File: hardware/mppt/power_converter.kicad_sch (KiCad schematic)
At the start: 25 parts, among them J301 Conn_01x01, J302 Conn_01x01, J303 CT3151, J304 CT3151, J305 CT3151, J306 CT3151, J307 Conn_01x01, J308 Conn_01x01

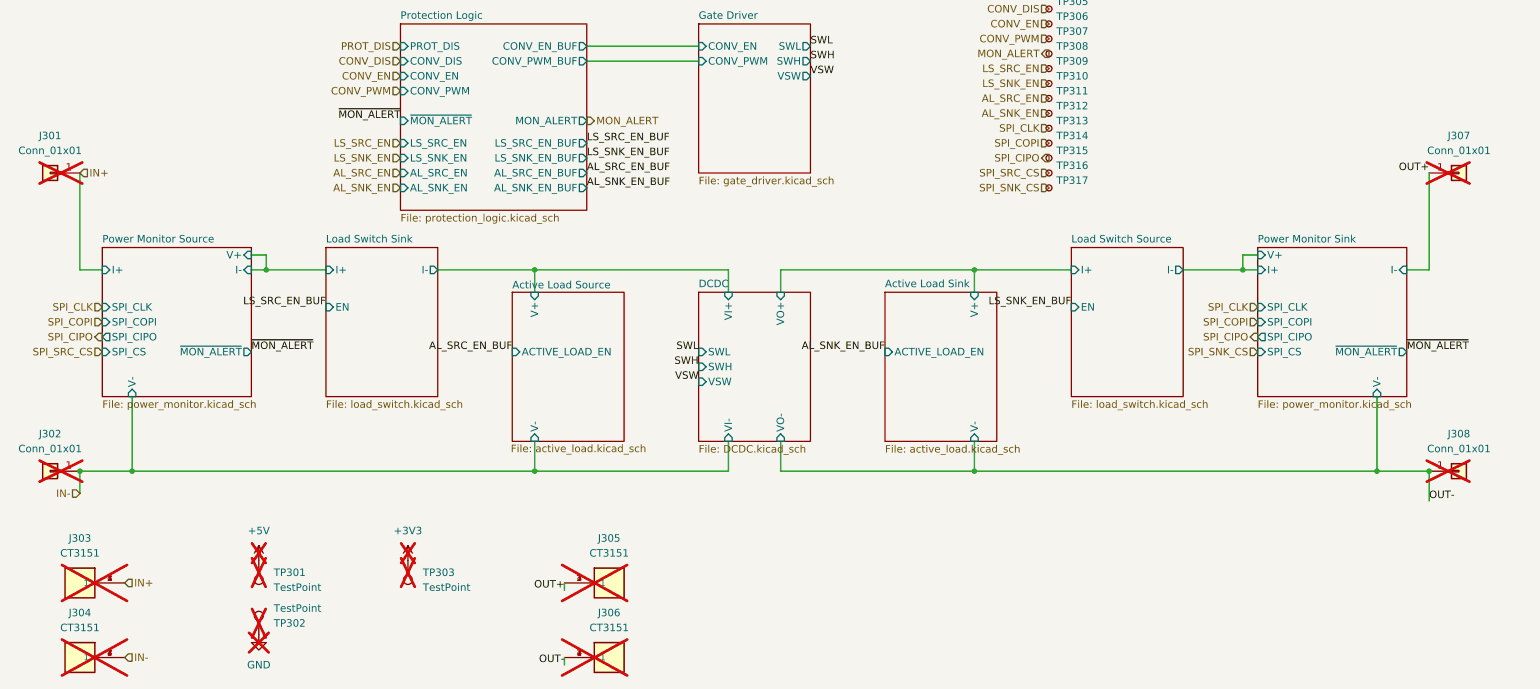
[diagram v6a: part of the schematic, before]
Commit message: converter schematic and layout.
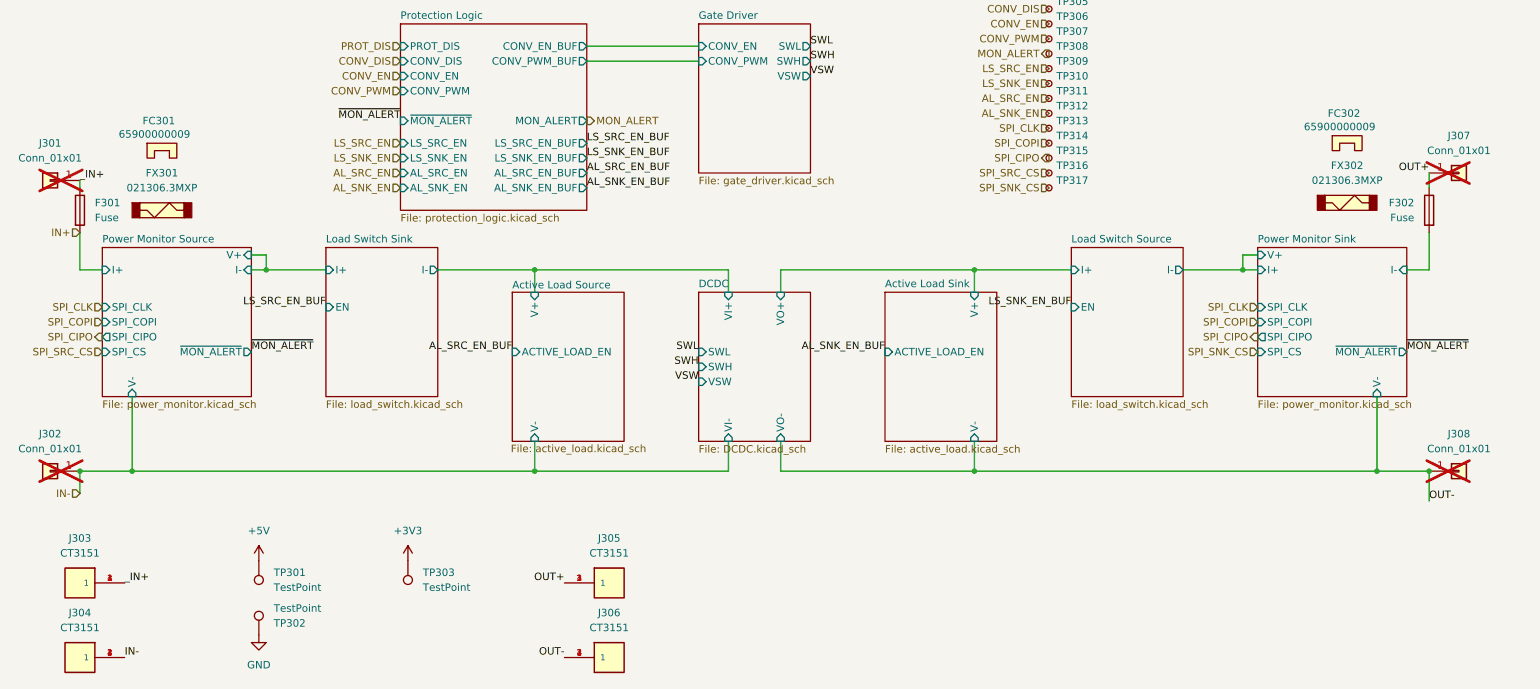
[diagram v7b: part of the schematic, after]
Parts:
- added F301, F302: Fuse, footprints:littelfuse_65600001009, symbol Device:Fuse
- added FC301, FC302: 65900000009, symbol littelfuse_021306_3MXP:65900000009
- added FX301, FX302: 021306.3MXP, symbol littelfuse_021306_3MXP:021306_3MXP
- J303, J304, J305, J306, TP301, TP302, TP303: now fitted; now in the parts list
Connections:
- net IN+: now also F301.2; no longer J301.1 (Pin_1), J303.1, J303.2 (1), J303.3 (1), J303.4 (1)
- net OUT+: now also F302.1
- new net Power Monitor Sink/I-: F302.2
- new net _IN+: F301.1, J301.1 (Pin_1), J303.1, J303.2 (1), J303.3 (1), J303.4 (1)

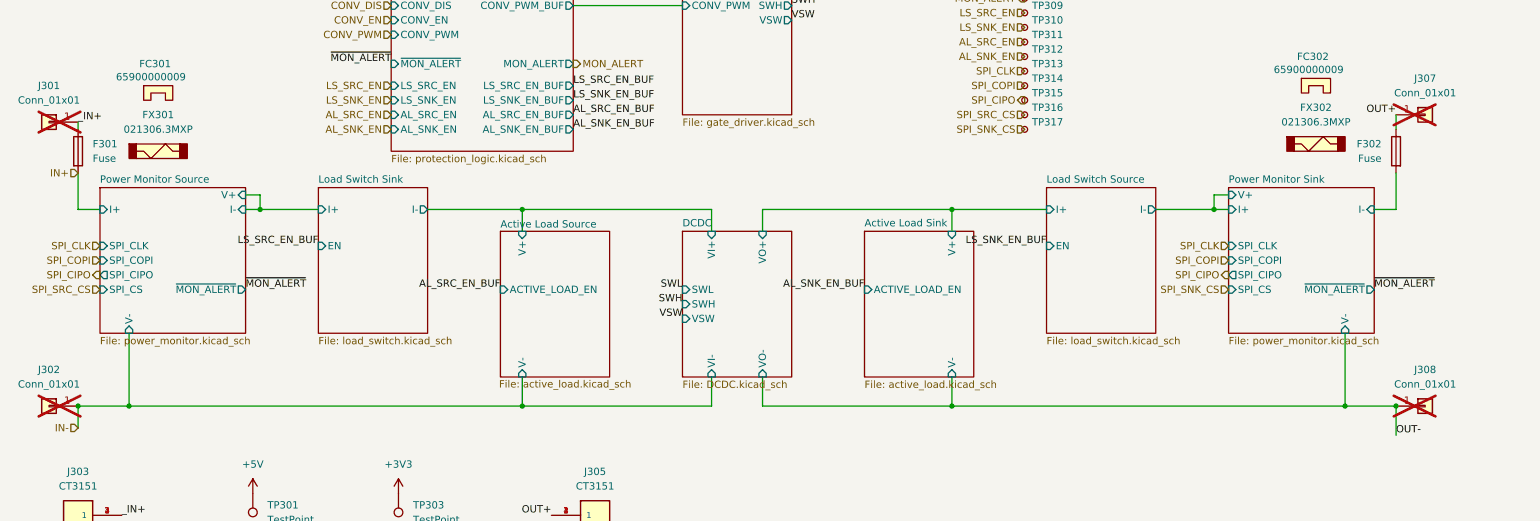
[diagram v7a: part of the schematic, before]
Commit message: unset dnp for all components in sch
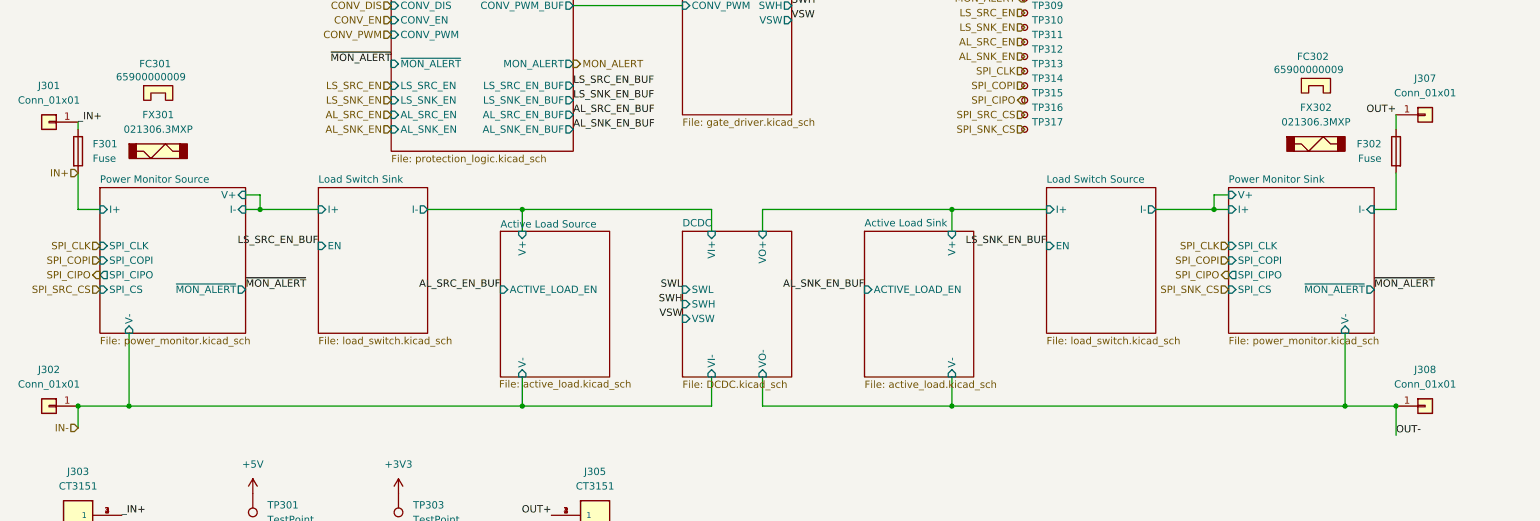
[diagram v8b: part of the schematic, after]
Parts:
- J301, J302, J307, J308: now fitted; now in the parts list
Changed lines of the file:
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@@
 		(exclude_from_sim no)
 		(in_bom yes)
-		(on_board no)
+		(on_board yes)
 		(dnp no)
 		(fields_autoplaced yes)
@@
 		(unit 1)
 		(exclude_from_sim no)
-		(in_bom no)
-		(on_board no)
-		(dnp yes)
+		(in_bom yes)
+		(on_board yes)
+		(dnp no)
 		(property "Reference" "J307"
 			(at 259.08 107.95 0)
@@
 		(exclude_from_sim no)
 		(in_bom yes)
-		(on_board no)
+		(on_board yes)
 		(dnp no)
 		(property "Reference" "FC301"
@@
 		(exclude_from_sim no)
 		(in_bom yes)
-		(on_board no)
+		(on_board yes)
 		(dnp no)
 		(fields_autoplaced yes)
@@
 		(unit 1)
 		(exclude_from_sim no)
-		(in_bom no)
-		(on_board no)
-		(dnp yes)
+		(in_bom yes)
+		(on_board yes)
+		(dnp no)
 		(property "Reference" "J308"
 			(at 259.08 158.75 0)
@@
 		(exclude_from_sim no)
 		(in_bom yes)
-		(on_board no)
+		(on_board yes)
 		(dnp no)
 		(property "Reference" "FC302"
@@
 		(unit 1)
 		(exclude_from_sim no)
-		(in_bom no)
-		(on_board no)
-		(dnp yes)
+		(in_bom yes)
+		(on_board yes)
+		(dnp no)
 		(fields_autoplaced yes)
 		(property "Reference" "J302"
@@
 		(unit 1)
 		(exclude_from_sim no)
-		(in_bom no)
-		(on_board no)
-		(dnp yes)
+		(in_bom yes)
+		(on_board yes)
+		(dnp no)
 		(fields_autoplaced yes)
 		(property "Reference" "J301"
